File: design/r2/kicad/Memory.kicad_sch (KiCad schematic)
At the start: 10 parts, among them U1 SST39SF040, U2 SST39SF040, U3 AS6C4008-55PCN, U4 AS6C4008-55PCN

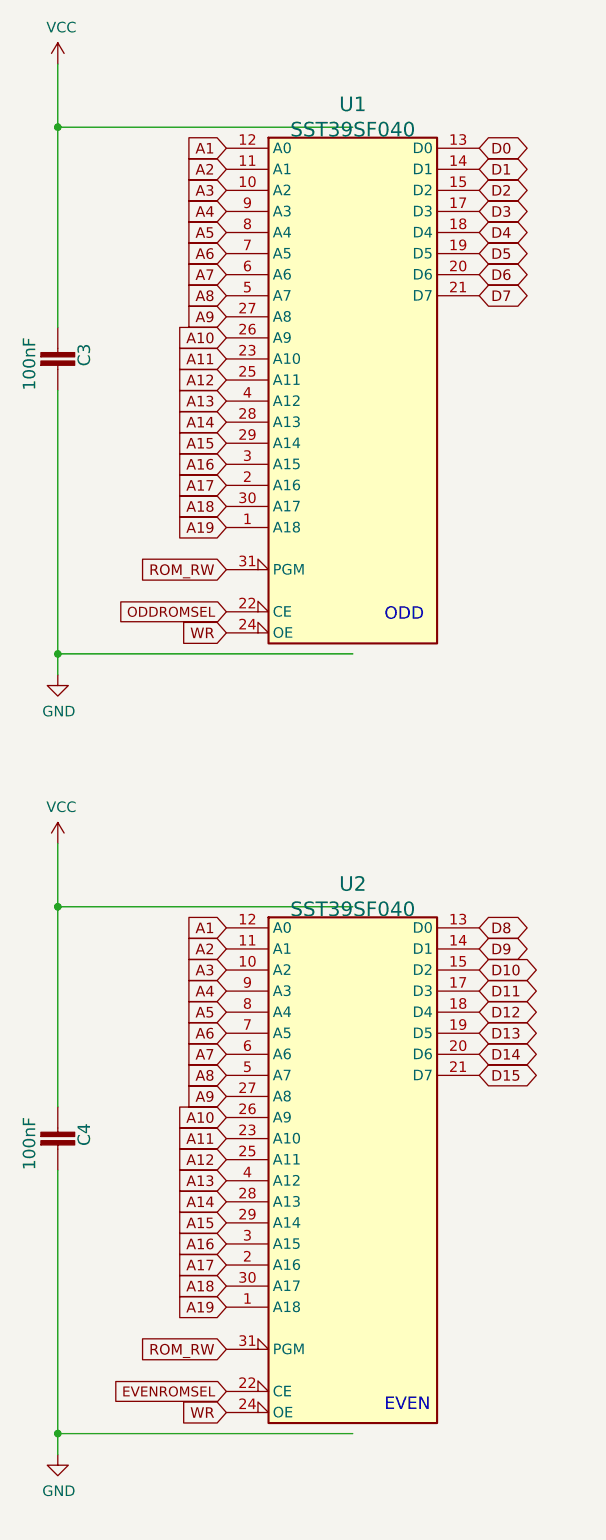
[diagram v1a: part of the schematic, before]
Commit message: Chore/merge 2.42 release master (#403)
* Feture/release 2.4 roll develop (#369)

* Roll 2.4 release

* Roll 2.5.dev

* Roll 2.5.dev release (#370)

* ignore files/dirs starting with dot, tweak prompt

* Ignore static libs

* ROM kernel: initial integration

* Add FW tests to CI

* Add <vector> include

* 🤷 Try fix GITHUB_WORKSPACE thing [3]

* Revert "🤷 Try fix GITHUB_WORKSPACE thing [3]"

This reverts commit 4369599145c125a8a3ae4daa409131a3e2088630.

* Revert "Add FW tests to CI"

This reverts commit 4073f7178b6fe7a046a48ebc25fbea2ce17a4f9d.

* Test in CI, take 2 🤞

* Include user.mk

* Make program responsible for pmm setup

* Change usgae message

* Don't use impl-reserved ids

* Flush all read/writes to stdio

* Cleanup Outdated Equates (#377)

* Remove equates.S

* Remove revision-specific defines from public
Except for MFP, which is the only place that IOBASE was actually used

* Fix comment about equates.S

* Delete firmware attic (#379)

* Fix #359 (#378)

* Feature/gdb lib (#381)

* Add GDB remote debugging support as a library

* Us FSINFO hints

* Fix outdated IC14 reference (#384)

* Fix outdated IC14 reference
* Use reference instead of hardcoding

* Update README.md (#386)

* Feature/68000 probe support (#387)

* Support device probes on 68000

* Switch default CPU to 68000

* Disable memcheck on 68000

* Don't (ab)use SDB_STATUS for BERR_HANDLER return

* Replace nasty label address hack

* Consistently use INSTALL_TEMP_BERR_HANDLER

* Update typos in documentation

* Fix SD Card write failures by increasing timeout

* Feature/kicad 7 (#388)

* Update r2 to Kicad 7
* Update r2020 to Kicad 7
* Complete Kicad 7 migration

* Update README.md

* Feature/swap tx rx again (#395)

* Swap TX/RX & CTS/RTS silkscreen r2

* Swap over labels
* Add arrows
* Some board tidy up

* Swap TX/RX & CTS/RTS silkscreen r2020

    * Swap over labels
    * Add arrows
    *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
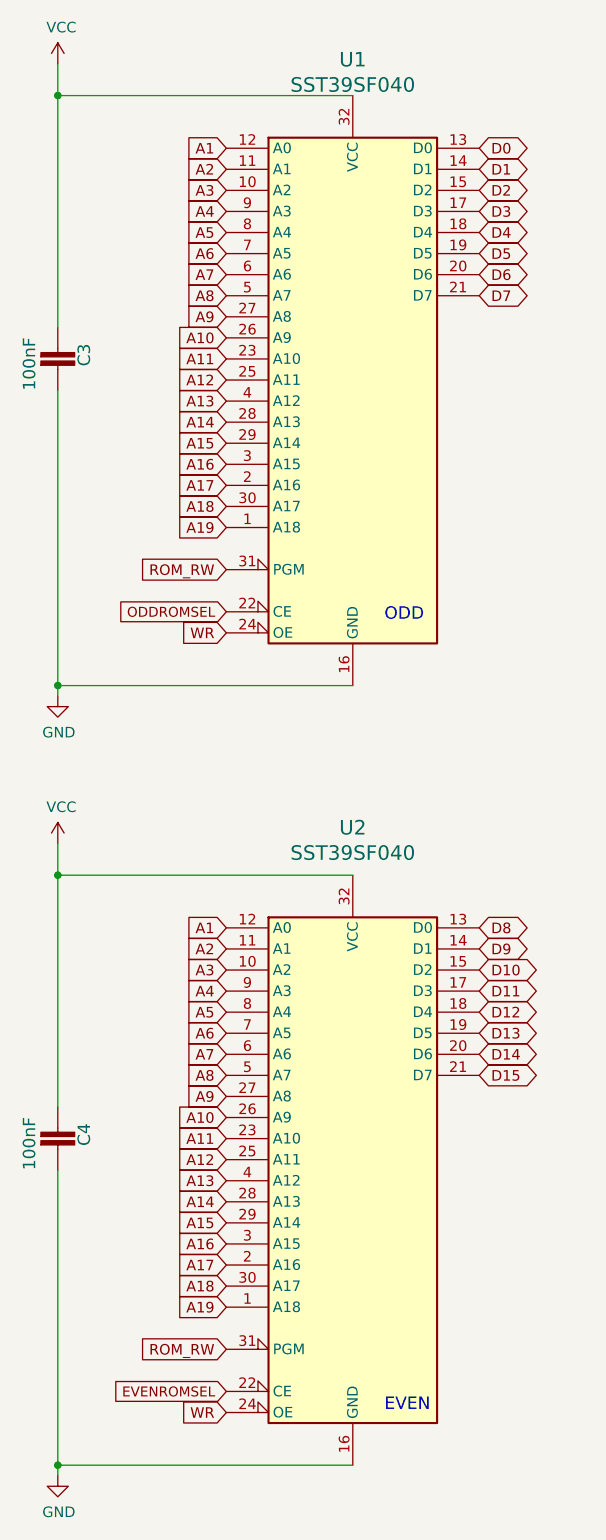
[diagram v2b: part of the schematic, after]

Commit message: Feature/smd birdseed (#427)
* GAL changes to better support coprocessor

* Update designs for copro GAL change

* Revert accidental DUARTSEL changes

* Re-add mistakenly-removed polarity symbols

* Tentative r2 SMD design

* Resize tiny resistors

* More address lines into GALs

* Reroute for FTDI

* prod

* Correct FT2232HL part number

* Mask expansion and silk tidy after first spin
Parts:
- C3, C4, C5, C6: footprint rosco_m68k:C2.5-3 -> Capacitor_SMD:C_0603_1608Metric
- R11: footprint rosco_m68k:0207_10 -> Resistor_SMD:R_0603_1608Metric
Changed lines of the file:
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@@
   (title_block
     (title "ROSCO_M68K GENERAL PURPOSE MC68010 COMPUTER")
-    (date "2024-03-09")
+    (date "2024-04-15")
     (rev "2.2")
     (company "The Really Old-School Company Limited")
@@
       (effects (font (size 1.27 1.27)) (justify left))
     )
-    (property "Footprint" "rosco_m68k:0207_10" (at 134.112 129.54 90)
+    (property "Footprint" "Resistor_SMD:R_0603_1608Metric" (at 134.112 129.54 90)
       (effects (font (size 1.27 1.27)) hide)
     )
@@
       (effects (font (size 1.4986 1.4986)) (justify left bottom))
     )
-    (property "Footprint" "rosco_m68k:C2.5-3" (at 25.4 149.86 0)
+    (property "Footprint" "Capacitor_SMD:C_0603_1608Metric" (at 25.4 149.86 0)
       (effects (font (size 1.27 1.27)) hide)
     )
@@
       (effects (font (size 1.4986 1.4986)) (justify left bottom))
     )
-    (property "Footprint" "rosco_m68k:C2.5-3" (at 115.57 57.15 0)
+    (property "Footprint" "Capacitor_SMD:C_0603_1608Metric" (at 115.57 57.15 0)
       (effects (font (size 1.27 1.27)) hide)
     )
@@
       (effects (font (size 1.4986 1.4986)) (justify left bottom))
     )
-    (property "Footprint" "rosco_m68k:C2.5-3" (at 201.93 57.15 0)
+    (property "Footprint" "Capacitor_SMD:C_0603_1608Metric" (at 201.93 57.15 0)
       (effects (font (size 1.27 1.27)) hide)
     )
@@
       (effects (font (size 1.4986 1.4986)) (justify left bottom))
     )
-    (property "Footprint" "rosco_m68k:C2.5-3" (at 25.4 55.88 0)
-      (effects (font (size 1.27 1.27)) hide)
-    )
+    (property "Footprint" "Capacitor_SMD:C_0603_1608Metric" (at 25.4 55.88 0)
+      (effects (font (size 1.27 1.27)) hide)
+    )
